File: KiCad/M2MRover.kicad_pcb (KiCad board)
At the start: 2 copper layers, 80 x 90 mm, 58 parts, among them J1 microbit_edge_connector, J10 Ultrasonic Forward, J2 Left Motor, J3 Right Motor, J4 Serial (Bluetooth), J5 MPU6050 Gyro & Acc GY-521, J6 Compass GY-273, J7 Light Detection, J8 Servo, J9 Ultrasonic Down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

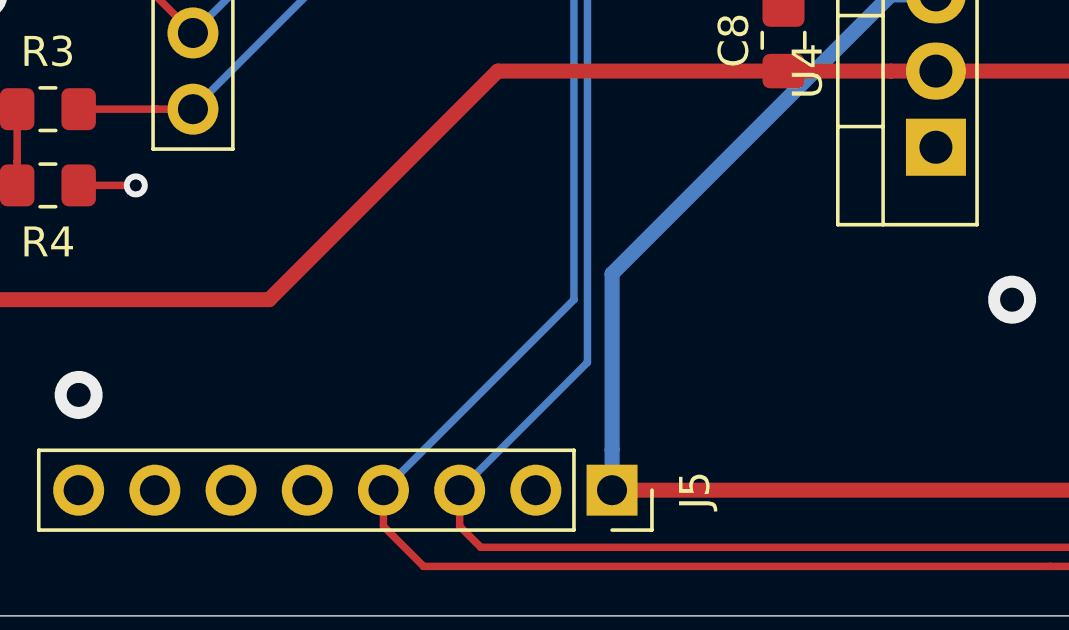
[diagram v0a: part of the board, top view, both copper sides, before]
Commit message: Add Software Cornwall logo to silk layer
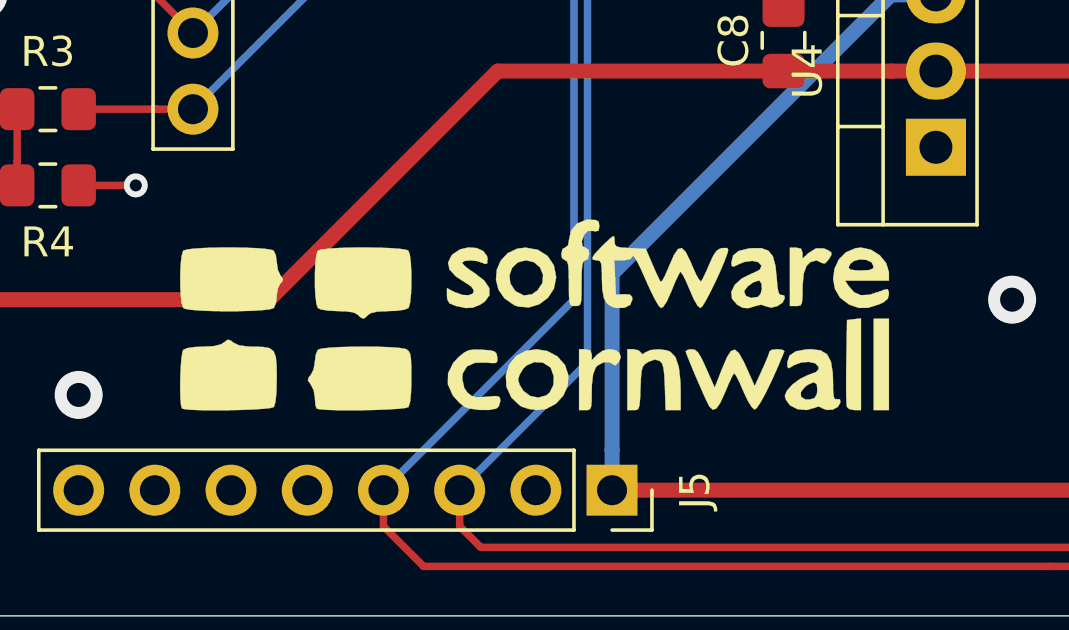
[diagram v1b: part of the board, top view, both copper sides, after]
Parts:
- added G***: LOGO, Software_Cornwall:SoftwareCornwallLogo, F.Cu at (134.6, 125.1)

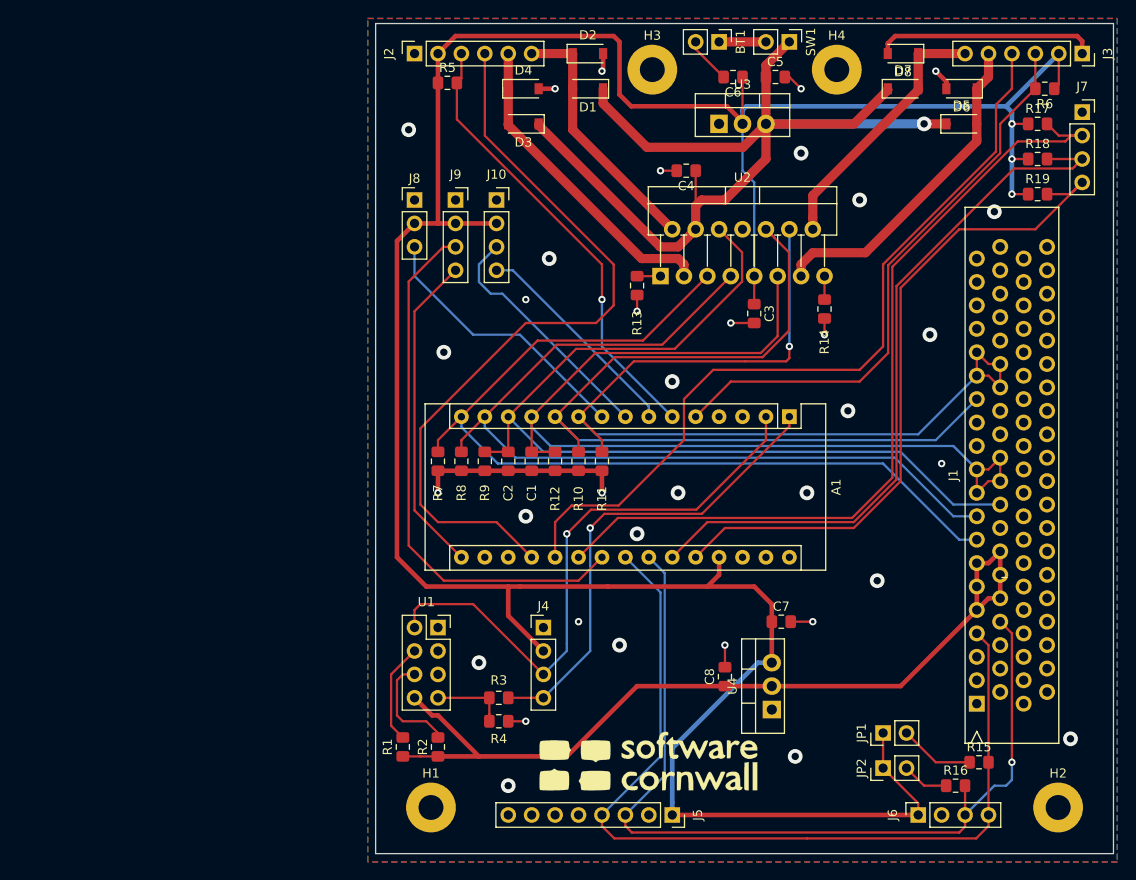
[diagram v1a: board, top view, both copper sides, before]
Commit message: Add pull up resistor to ESP8266 GPIO0 and remove GND tracks
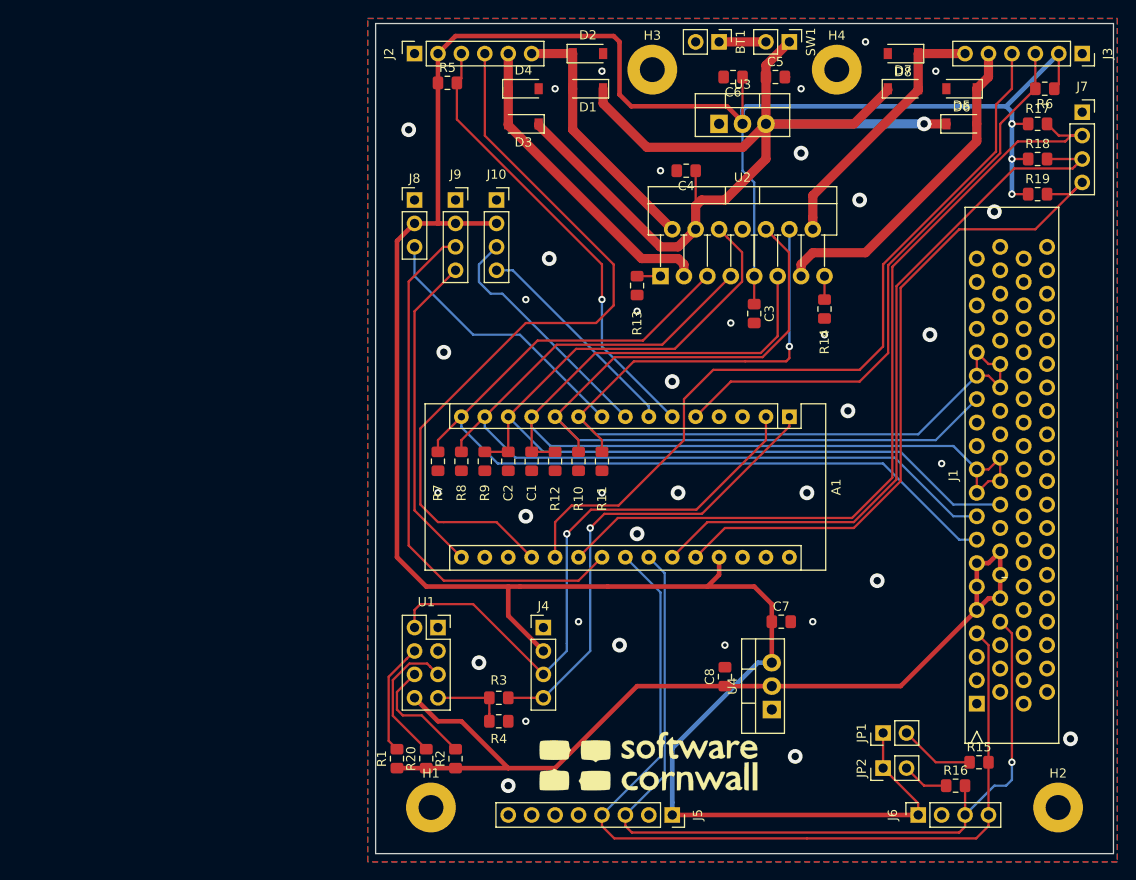
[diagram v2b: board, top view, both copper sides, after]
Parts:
- added R20: 10K, Resistor_SMD:R_0805_2012Metric_Pad1.15x1.40mm_HandSolder, F.Cu at (110.5, 124.7)
- moved R2 2.29 mm to (113.7, 124.7)
- moved R1 1.42 mm to (107.3, 124.7)
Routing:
- net GND: track 74.6 -> 1.45 mm, vias 35 -> 36
- net Net-(R20-Pad2): track 0.00 -> 15.1 mm
- net +3V3: track 94.7 -> 99.6 mm
- net Net-(R1-Pad2): track 11.0 -> 12.2 mm
- net Net-(R2-Pad2): track 11.7 -> 12.7 mm

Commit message: Add Software Cornwall Log via symbol
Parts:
- removed G***: LOGO, Software_Cornwall:SoftwareCornwallLogo
- added LOGO1: Software_Cornwall_Logo, Software_Cornwall:SoftwareCornwallLogo, F.Cu at (134.6, 125.1)
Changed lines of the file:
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@@
-(kicad_pcb (version 20171130) (host pcbnew "(5.1.4)-1")
+(kicad_pcb (version 20171130) (host pcbnew 5.1.4-e60b266~84~ubuntu18.04.1)
   (general
     (thickness 1.6)
@@
     (add_net Ultrasonic_Forward_Trigger)
   )
-  (module Resistor_SMD:R_0805_2012Metric_Pad1.15x1.40mm_HandSolder (layer F.Cu)
-    (at 110.49 124.705 90)
-    (descr "Resistor SMD 0805 (2012 Metric), square (rectangular) end terminal, IPC_7351 nominal with elongated pad for handsoldering. (Body size source: https://docs.google.com/spreadsheets/d/1BsfQQcO9C6DZCsRaXUlFlo91Tg2WpOkGARC1WS5S8t0/edit?usp=sharing), generated with kicad-footprint-generator")
-    (tags "resistor handsolder")
-    (attr smd)
-    (fp_text reference R20 (at 0 -1.65 90) (layer F.SilkS)
-      (effects (font (size 1 1) (thickness 0.15)))
-    )
-    (fp_text value 10K (at 0 1.65 90) (layer F.Fab)
-      (effects (font (size 1 1) (thickness 0.15)))
-    )
-    (fp_text user %R (at 0 0 90) (layer F.Fab)
-      (effects (font (size 0.5 0.5) (thickness 0.08)))
-    )
-    (fp_line (start 1.85 0.95) (end -1.85 0.95) (layer F.CrtYd) (width 0.05))
-    (fp_line (start 1.85 -0.95) (end 1.85 0.95) (layer F.CrtYd) (width 0.05))
-    (fp_line (start -1.85 -0.95) (end 1.85 -0.95) (layer F.CrtYd) (width 0.05))
-    (fp_line (start -1.85 0.95) (end -1.85 -0.95) (layer F.CrtYd) (width 0.05))
-    (fp_line (start -0.261252 0.71) (end 0.261252 0.71) (layer F.SilkS) (width 0.12))
-    (fp_line (start -0.261252 -0.71) (end 0.261252 -0.71) (layer F.SilkS) (width 0.12))
-    (fp_line (start 1 0.6) (end -1 0.6) (layer F.Fab) (width 0.1))
-    (fp_line (start 1 -0.6) (end 1 0.6) (layer F.Fab) (width 0.1))
-    (fp_line (start -1 -0.6) (end 1 -0.6) (layer F.Fab) (width 0.1))
-    (fp_line (start -1 0.6) (end -1 -0.6) (layer F.Fab) (width 0.1))
-    (pad 2 smd roundrect (at 1.025 0 90) (size 1.15 1.4) (layers F.Cu F.Paste F.Mask) (roundrect_rratio 0.217391)
-      (net 103 "Net-(R20-Pad2)"))
-    (pad 1 smd roundrect (at -1.025 0 90) (size 1.15 1.4) (layers F.Cu F.Paste F.Mask) (roundrect_rratio 0.217391)
-      (net 30 +3V3))
-    (model ${KISYS3DMOD}/Resistor_SMD.3dshapes/R_0805_2012Metric.wrl
-      (at (xyz 0 0 0))
-      (scale (xyz 1 1 1))
-      (rotate (xyz 0 0 0))
-    )
-  )
   (module Software_Cornwall:SoftwareCornwallLogo (layer F.Cu)
     (at 134.62 125.095)
-    (fp_text reference G*** (at 0 0) (layer F.SilkS) hide
+    (fp_text reference LOGO1 (at 0 0) (layer F.SilkS) hide
       (effects (font (size 1.524 1.524) (thickness 0.3)))
     )
-    (fp_text value LOGO (at 0.75 0) (layer F.SilkS) hide
+    (fp_text value Software_Cornwall_Logo (at 0.75 0) (layer F.SilkS) hide
       (effects (font (size 1.524 1.524) (thickness 0.3)))
     )
@@
       (xy -10.165327 0.727294)) (layer F.SilkS) (width 0.01))
   )
+  (module Resistor_SMD:R_0805_2012Metric_Pad1.15x1.40mm_HandSolder (layer F.Cu)
+    (at 110.49 124.705 90)
+    (descr "Resistor SMD 0805 (2012 Metric), square (rectangular) end terminal, IPC_7351 nominal with elongated pad for handsoldering. (Body size source: https://docs.google.com/spreadsheets/d/1BsfQQcO9C6DZCsRaXUlFlo91Tg2WpOkGARC1WS5S8t0/edit?usp=sharing), generated with kicad-footprint-generator")
+    (tags "resistor handsolder")
+    (attr smd)
+    (fp_text reference R20 (at 0 -1.65 90) (layer F.SilkS)
+      (effects (font (size 1 1) (thickness 0.15)))
+    )
+    (fp_text value 10K (at 0 1.65 90) (layer F.Fab)
+      (effects (font (size 1 1) (thickness 0.15)))
+    )
+    (fp_text user %R (at 0 0 90) (layer F.Fab)
+      (effects (font (size 0.5 0.5) (thickness 0.08)))
+    )
+    (fp_line (start 1.85 0.95) (end -1.85 0.95) (layer F.CrtYd) (width 0.05))
+    (fp_line (start 1.85 -0.95) (end 1.85 0.95) (layer F.CrtYd) (width 0.05))
+    (fp_line (start -1.85 -0.95) (end 1.85 -0.95) (layer F.CrtYd) (width 0.05))
+    (fp_line (start -1.85 0.95) (end -1.85 -0.95) (layer F.CrtYd) (width 0.05))
+    (fp_line (start -0.261252 0.71) (end 0.261252 0.71) (layer F.SilkS) (width 0.12))
+    (fp_line (start -0.261252 -0.71) (end 0.261252 -0.71) (layer F.SilkS) (width 0.12))
+    (fp_line (start 1 0.6) (end -1 0.6) (layer F.Fab) (width 0.1))
+    (fp_line (start 1 -0.6) (end 1 0.6) (layer F.Fab) (width 0.1))
+    (fp_line (start -1 -0.6) (end 1 -0.6) (layer F.Fab) (width 0.1))
+    (fp_line (start -1 0.6) (end -1 -0.6) (layer F.Fab) (width 0.1))
+    (pad 2 smd roundrect (at 1.025 0 90) (size 1.15 1.4) (layers F.Cu F.Paste F.Mask) (roundrect_rratio 0.217391)
+      (net 103 "Net-(R20-Pad2)"))
+    (pad 1 smd roundrect (at -1.025 0 90) (size 1.15 1.4) (layers F.Cu F.Paste F.Mask) (roundrect_rratio 0.217391)
+      (net 30 +3V3))
+    (model ${KISYS3DMOD}/Resistor_SMD.3dshapes/R_0805_2012Metric.wrl
+      (at (xyz 0 0 0))
+      (scale (xyz 1 1 1))
+      (rotate (xyz 0 0 0))
+    )
+  )
   (module Module:Arduino_Nano (layer F.Cu)

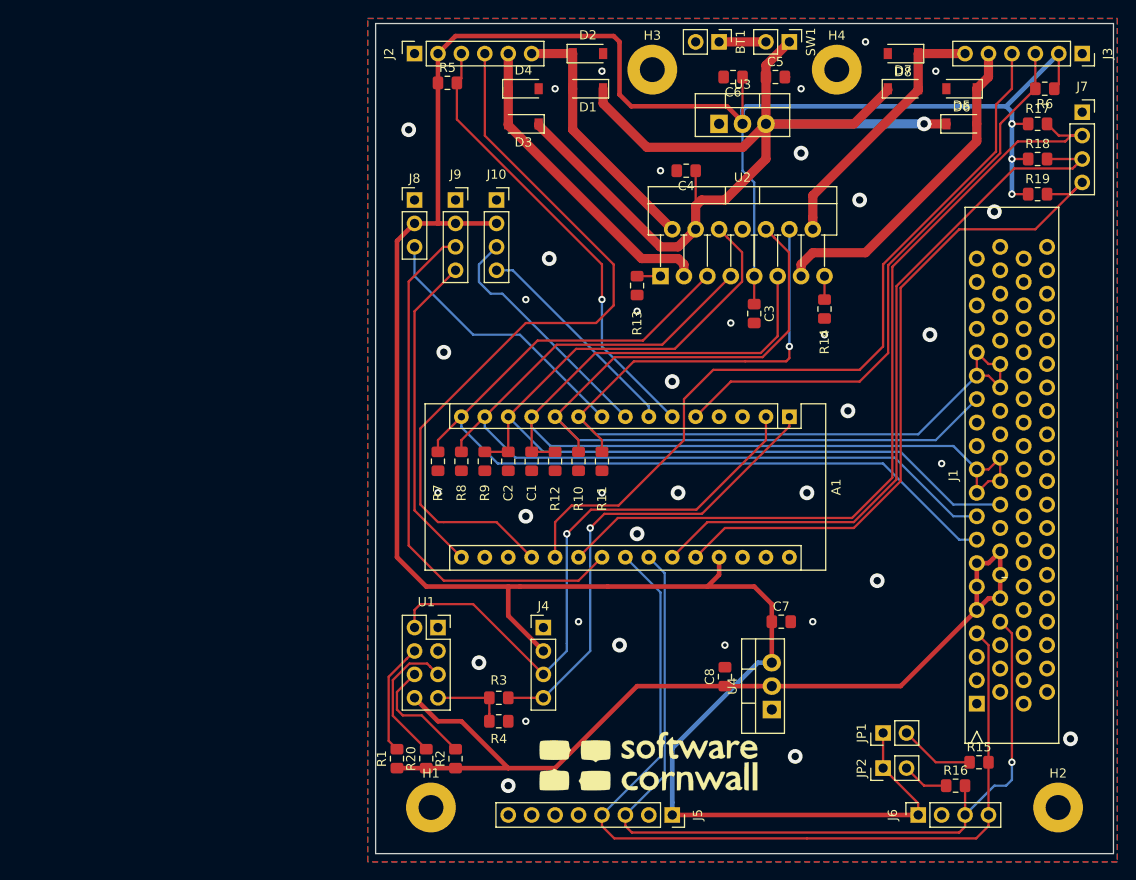
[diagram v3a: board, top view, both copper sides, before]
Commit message: Move 5V regulator to stop physical clash
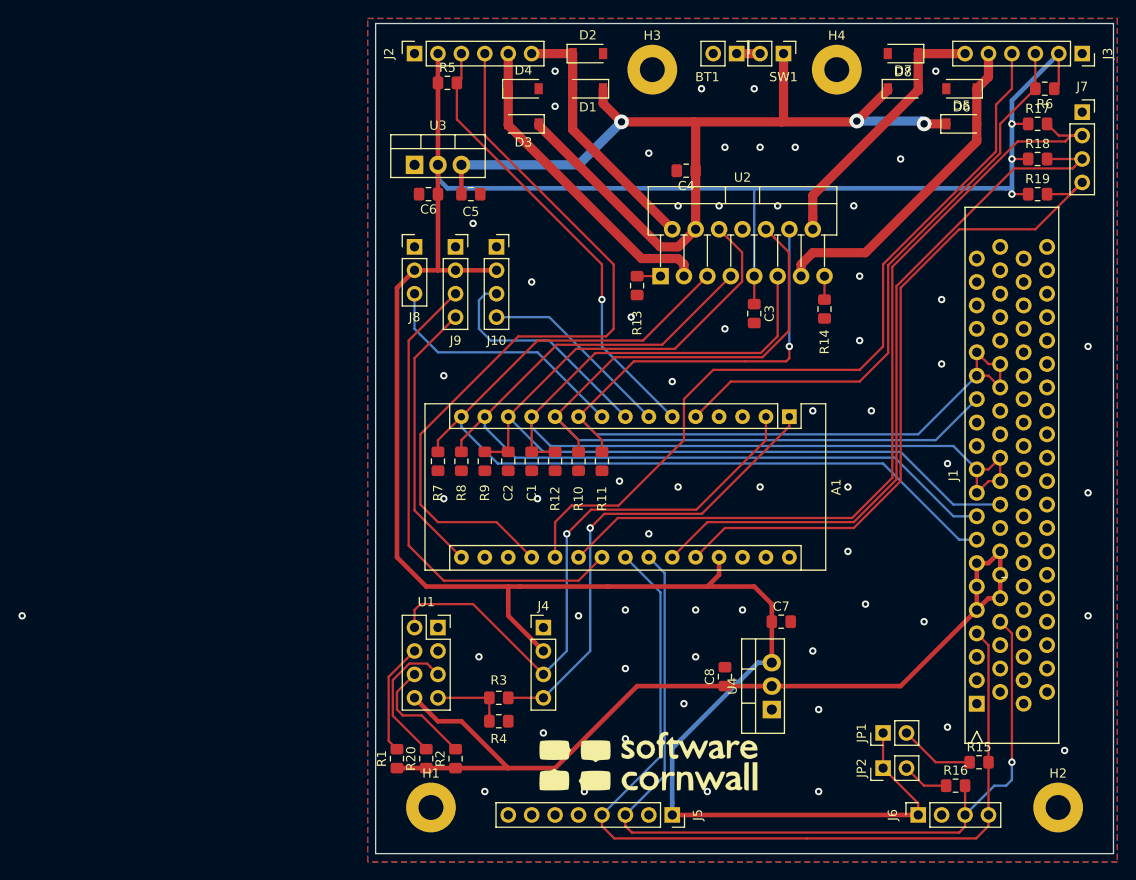
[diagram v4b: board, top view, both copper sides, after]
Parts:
- moved C5 35.4 mm to (115.3, 63.5)
- moved C6 35.4 mm to (110.7, 63.5)
- moved U3 33.3 mm to (109.2, 60.3)
- moved J10 5.08 mm to (118.1, 69.2)
- moved J8 5.08 mm to (109.2, 69.2)
- moved J9 5.08 mm to (113.7, 69.2)
- moved BT1 2.29 mm to (144.1, 48.3)
- moved SW1 1.42 mm to (149.2, 48.3)
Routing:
- net +5V: track 308.4 -> 288.0 mm
- net Ultrasonic_Down_Echo: track 58.8 -> 53.0 mm
- net Ultrasonic_Down_Trigger: track 35.1 -> 30.0 mm
- net Ultrasonic_Forward_Trigger: track 23.7 -> 21.0 mm
- net +BATT: track 112.5 -> 109.8 mm, vias 1 -> 3
- net Net-(BT1-Pad1): track 5.08 -> 2.54 mm
- net Servo: track 29.8 -> 28.1 mm
- net GND: track 1.45 -> 0.00 mm, vias 36 -> 58
- net Ultrasonic_Forward_Echo: track 26.5 -> 25.1 mm
- net Left_LED: track 82.3 -> 83.4 mm
- net (no net): vias 0 -> 1

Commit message: Add JLCPCB order number to silk
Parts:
- added ORDERNO1: JLCPCB_Order_Number, Software_Cornwall:JLCPCBOrderNumber, F.Cu at (141.6, 92.7)
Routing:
- net (no net): vias 1 -> 0
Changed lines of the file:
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@@
     (thickness 1.6)
     (drawings 11)
-    (tracks 416)
+    (tracks 415)
     (zones 0)
-    (modules 60)
+    (modules 61)
     (nets 104)
   )
@@
     (0 F.Cu signal)
     (31 B.Cu signal)
-    (33 F.Adhes user)
+    (33 F.Adhes user hide)
     (35 F.Paste user)
     (37 F.SilkS user)
@@
   )
   (setup
-    (last_trace_width 1)
+    (last_trace_width 0.25)
     (user_trace_width 0.5)
     (user_trace_width 1)
@@
     (add_net Ultrasonic_Forward_Trigger)
   )
+  (module Software_Cornwall:JLCPCBOrderNumber (layer F.Cu)
+    (at 141.605 92.71)
+    (fp_text reference ORDERNO1 (at 0 2.54) (layer F.SilkS) hide
+      (effects (font (size 1 1) (thickness 0.15)))
+    )
+    (fp_text value JLCPCB_Order_Number (at 0 -2.54) (layer F.Fab) hide
+      (effects (font (size 1 1) (thickness 0.15)))
+    )
+    (fp_text user JLCJLCJLCJLC (at 0 0) (layer F.SilkS)
+      (effects (font (size 1.5 1.5) (thickness 0.15)))
+    )
+  )
   (module Software_Cornwall:SoftwareCornwallLogo (layer F.Cu)
     (at 134.62 125.095)
@@
   (gr_line (start 185 45) (end 185 135) (layer Edge.Cuts) (width 0.05))
   (gr_line (start 105 45) (end 185 45) (layer Edge.Cuts) (width 0.05))
-  (via (at 66.675 109.22) (size 0.8) (drill 0.4) (layers F.Cu B.Cu) (net 0))
   (via (at 165.735 50.165) (size 0.8) (drill 0.4) (layers F.Cu B.Cu) (net 1))
   (via (at 112.395 96.52) (size 0.8) (drill 0.4) (layers F.Cu B.Cu) (net 1))
